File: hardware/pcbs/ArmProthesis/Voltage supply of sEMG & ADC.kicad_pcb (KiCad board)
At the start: 4 copper layers, 51.1 x 56.5 mm, 69 parts, among them Q1 BC817, Q2 BC817, Q3 BC817, U1 LT3045xMSE, U2 TPS7A4701RGWR, U3 LT8471EFE_TRPBF, U4 LT3094xMSE

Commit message: .
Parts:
- moved L3 0.99 mm to (117.3, 74.3)
- moved C5 0.98 mm to (118.0, 78.0)
- moved R17 0.30 mm to (112.9, 72.9)
- moved R1 0.29 mm to (103.5, 82.0)
- moved R15 0.12 mm to (121.7, 55.4)
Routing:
- net GND: track 85.2 -> 83.2 mm, vias 60 -> 57
- net Net-(U3-PG1): track 14.0 -> 13.4 mm

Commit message: BMS v0.5 still not resized
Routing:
- added copper zone on F.Cu, net Net-(U3-C3)
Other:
- board text added: "bigger gnd"
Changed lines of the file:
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@@
+		)
+	)
+	(gr_text "bigger gnd"
+		(at 120.26 81.055 0)
+		(layer "Cmts.User")
+		(effects
+			(font
+				(size 1.5 1.5)
+				(thickness 0.3)
+				(bold yes)
+			)
+			(justify left bottom)
 		)
 	)
@@
 	(segment
 		(start 128 79.75)
-		(end 129.65 79.75)
+		(end 130.55 79.75)
 		(width 0.3)
 		(layer "F.Cu")
@@
 	)
 	(segment
-		(start 129.9 80)
+		(start 130.55 79.75)
+		(end 130.8 80)
+		(width 0.3)
+		(layer "F.Cu")
+		(net 6)
+	)
+	(segment
+		(start 130.8 80)
 		(end 131.3325 80)
-		(width 0.3)
-		(layer "F.Cu")
-		(net 6)
-	)
-	(segment
-		(start 129.65 79.75)
-		(end 129.9 80)
 		(width 0.3)
 		(layer "F.Cu")
@@
 	)
 	(segment
+		(start 130.099596 80.44)
+		(end 129.44 80.44)
+		(width 0.3)
+		(layer "F.Cu")
+		(net 7)
+	)
+	(segment
+		(start 120.990364 77.649)
+		(end 119.909 77.649)
+		(width 0.3)
+		(layer "F.Cu")
+		(net 7)
+	)
+	(segment
+		(start 129.44 80.44)
+		(end 129.4 80.4)
+		(width 0.3)
+		(layer "F.Cu")
+		(net 7)
+	)
+	(segment
+		(start 121.141364 77.8)
+		(end 120.990364 77.649)
+		(width 0.3)
+		(layer "F.Cu")
+		(net 7)
+	)
+	(segment
+		(start 129.8 77.2)
+		(end 129.2 77.8)
+		(width 0.3)
+		(layer "F.Cu")
+		(net 7)
+	)
+	(segment
+		(start 119.624975 78.025025)
+		(end 118.899975 78.025025)
+		(width 0.3)
+		(layer "F.Cu")
+		(net 7)
+	)
+	(segment
+		(start 119.909 77.649)
+		(end 119.955 77.695)
+		(width 0.3)
+		(layer "F.Cu")
+		(net 7)
+	)
+	(segment
 		(start 129.4 80.4)
 		(end 128 80.4)
-		(width 0.3)
-		(layer "F.Cu")
-		(net 7)
-	)
-	(segment
-		(start 120.990364 77.649)
-		(end 119.909 77.649)
-		(width 0.3)
-		(layer "F.Cu")
-		(net 7)
-	)
-	(segment
-		(start 121.141364 77.8)
-		(end 120.990364 77.649)
-		(width 0.3)
-		(layer "F.Cu")
-		(net 7)
-	)
-	(segment
-		(start 129.8 77.2)
-		(end 129.2 77.8)
-		(width 0.3)
-		(layer "F.Cu")
-		(net 7)
-	)
-	(segment
-		(start 119.624975 78.025025)
-		(end 118.899975 78.025025)
-		(width 0.3)
-		(layer "F.Cu")
-		(net 7)
-	)
-	(segment
-		(start 119.909 77.649)
-		(end 119.955 77.695)
-		(width 0.3)
-		(layer "F.Cu")
-		(net 7)
-	)
-	(segment
-		(start 129.7 80.7)
-		(end 129.4 80.4)
 		(width 0.3)
 		(layer "F.Cu")
@@
 	)
 	(via
-		(at 129.7 80.7)
+		(at 130.099596 80.44)
 		(size 0.6)
 		(drill 0.3)
@@
 	)
 	(segment
+		(start 130.099596 80.44)
+		(end 130.099596 79.700404)
+		(width 0.3)
+		(layer "B.Cu")
+		(net 7)
+	)
+	(segment
+		(start 131.025 78.775)
+		(end 131.025 77.825)
+		(width 0.3)
+		(layer "B.Cu")
+		(net 7)
+	)
+	(segment
 		(start 129.975 77.2)
 		(end 129.375 77.8)
@@
 	)
 	(segment
-		(start 129.7 80.1)
+		(start 130.099596 79.700404)
 		(end 131.025 78.775)
+		(width 0.3)
+		(layer "B.Cu")
+		(net 7)
+	)
+	(segment
+		(start 131.025 77.825)
+		(end 130.4 77.2)
 		(width 0.3)
 		(layer "B.Cu")
@@
 	)
 	(segment
-		(start 129.7 80.7)
-		(end 129.7 80.1)
-		(width 0.3)
-		(layer "B.Cu")
-		(net 7)
-	)
-	(segment
 		(start 130.4 77.2)
 		(end 129.975 77.2)
-		(width 0.3)
-		(layer "B.Cu")
-		(net 7)
-	)
-	(segment
-		(start 131.025 78.775)
-		(end 131.025 77.825)
-		(width 0.3)
-		(layer "B.Cu")
-		(net 7)
-	)
-	(segment
-		(start 131.025 77.825)
-		(end 130.4 77.2)
 		(width 0.3)
 		(layer "B.Cu")
@@
 	)
 	(zone
+		(net 22)
+		(net_name "Net-(U3-C3)")
+		(layer "F.Cu")
+		(hatch edge 0.5)
+		(priority 1)
+		(connect_pads yes
+			(clearance 0)
+		)
+		(min_thickness 0.25)
+		(filled_areas_thickness no)
+		(fill yes
+			(thermal_gap 0.5)
+			(thermal_bridge_width 0.5)
+		)
+		(polygon
+			(pts
+				(xy 127.225 80.8) (xy 127.225 81.275) (xy 129.3 81.275) (xy 129.3 84.975) (xy 138.6 85) (xy 138.6 80.8)
+			)
+		)
+	)
+	(zone

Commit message: .
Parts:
- moved R4 4.12 mm to (111.3, 79.5), turned to -90 degrees
- moved C6 2.26 mm to (122.3, 70.8), turned to 0 degrees
- moved Cby5 2.04 mm to (128.5, 61.6)
- moved C7 1.18 mm to (127.6, 70.8)
- moved R20 0.95 mm to (122.5, 62.5), turned to 0 degrees
- moved C9 0.92 mm to (127.7, 72.8)
- moved C8 0.79 mm to (122.3, 72.8), turned to 0 degrees
- moved R25 0.45 mm to (112.9, 77.7)
- moved C2in1 0.21 mm to (113.4, 68.2)
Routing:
- net Net-(U3-FB2): track 12.1 -> 0.00 mm
- net /+5V: track 42.4 -> 32.3 mm
- net /+11.1V: track 10.7 -> 6.94 mm
- net GND: track 83.2 -> 79.8 mm, vias 57 -> 63
- net +6V: track 72.7 -> 70.6 mm, vias 4 -> 3
- net Net-(U1-PGFB): track 12.4 -> 14.4 mm
- net Net-(U3-PG1): track 13.4 -> 14.3 mm
- net Net-(U4-PGFB): track 18.6 -> 19.3 mm
- net Net-(U3-PG2): track 17.2 -> 16.5 mm
- added copper zone on F.Cu, net -6V
- added copper zone on F.Cu, net /+5V
- added copper zone on F.Cu, net GND
- added copper zone on F.Cu, net Net-(U3-E1)
- added copper zone on F.Cu, net Net-(U3-FB2)
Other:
- board text added: "SL-sEMG&ADC-PSU v0.5"
- board text removed: "SL-sEMG&ADC-PSU v0.4"
- board text removed: "bigger gnd"

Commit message: updates
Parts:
- added D8: DFLS240L, Diode_SMD:D_PowerDI-123, F.Cu at (88.6, 68.8)
- added D9: DFLS240, Diode_SMD:D_PowerDI-123, F.Cu at (131.4, 63.6)
- C1, Cby1, Cby3, Cby5, Cby7: value 10u -> 10uF
- C2, C3: value 100n -> 100nF
- Cby4: value 47u -> 47uF
- moved D7 1.71 mm to (136.6, 63.3)
- moved R22 1.71 mm to (133.0, 63.3)
- moved R15 1.30 mm to (123.0, 55.4)
- moved Cby6 1.03 mm to (124.8, 55.4)
- moved Cby5 0.41 mm to (128.1, 61.6)
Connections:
- L2 pad 2: -6V -> Net-(D9-K)
- R16 pad 1: -6V -> Net-(D9-K)
- U1 pad 12: /+5V -> Net-(U1-PG)
- U3 pad 19: -6V -> Net-(D9-K)
- U4 pad 12: /-5.5V -> Net-(U4-PG)
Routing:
- net GND: track 79.8 -> 76.4 mm, vias 63 -> 68
- net Net-(U4-SET): track 5.79 -> 4.73 mm

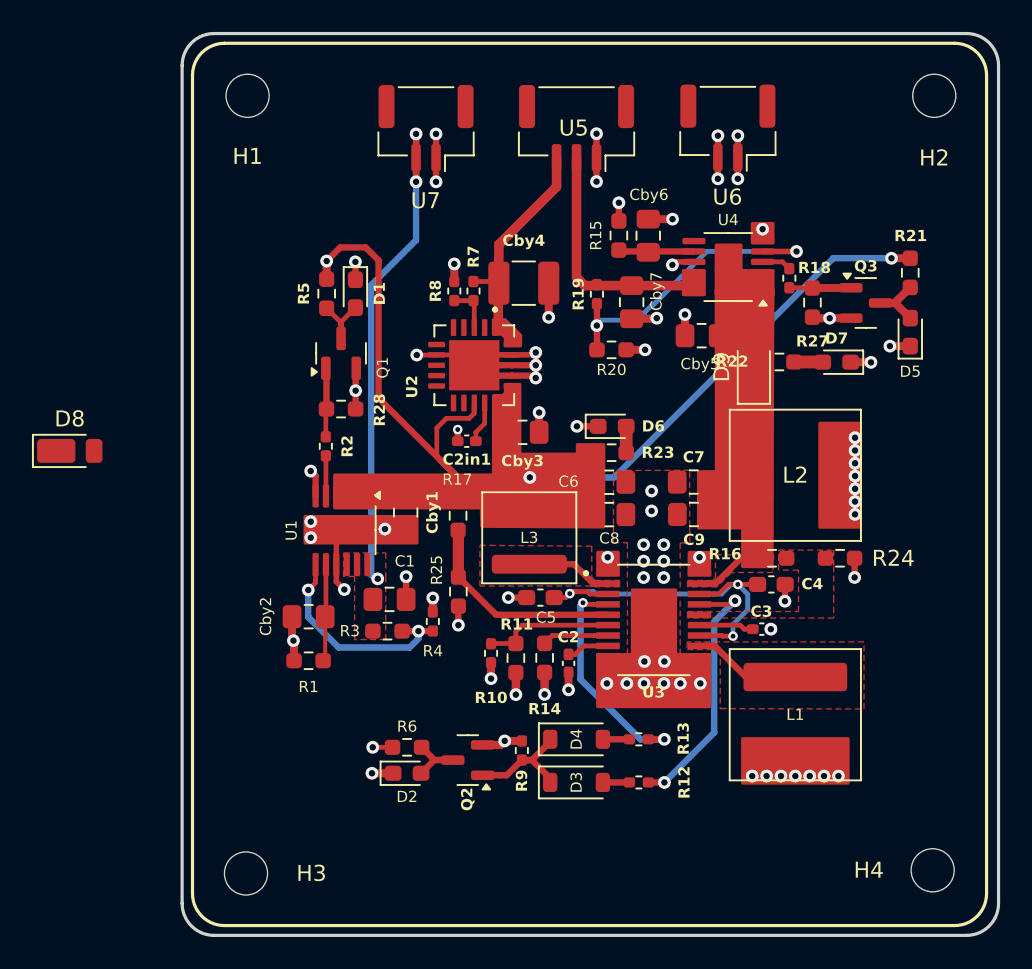
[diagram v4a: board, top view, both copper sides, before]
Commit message: Fix Vsupply
added important Schottky diodes on the BUCK
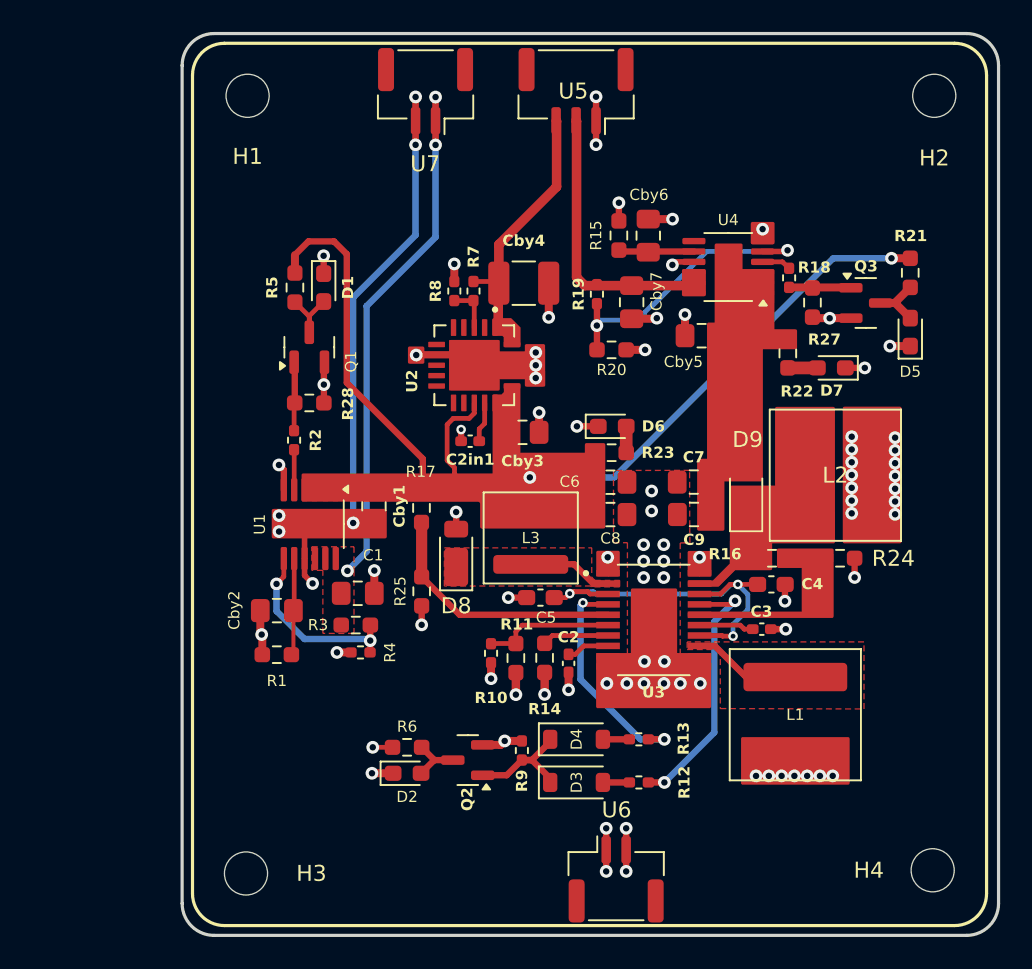
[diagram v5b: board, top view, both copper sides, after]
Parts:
- moved U6 47.6 mm to (122.8, 95.7), turned to 0 degrees
- moved D8 25.0 mm to (112.8, 75.3), turned to 90 degrees
- moved D9 7.99 mm to (130.9, 71.6)
- moved R4 4.93 mm to (106.8, 81.5), turned to 0 degrees
- moved L2 2.51 mm to (136.5, 70.4)
- moved R17 2.34 mm to (110.6, 72.4)
- moved U5 2.32 mm to (120.3, 46.3)
- moved U7 2.32 mm to (110.8, 46.3)
- moved R25 2.30 mm to (110.6, 77.6)
- moved C1 2.02 mm to (106.6, 77.8)
- moved R3 2.02 mm to (106.5, 79.7)
- moved R5 2.02 mm to (102.7, 58.6)
- moved R1 2.02 mm to (101.5, 81.6)
- moved U1 2.02 mm to (103.6, 73.4)
- moved Q1 2.02 mm to (103.6, 62.3)
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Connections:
- U1 pad 12: Net-(U1-PG) -> /+5V
- U4 pad 12: Net-(U4-PG) -> /-5.5V
- U7 pad 1: GND -> /+5V
- U7 pad 2: /+5V -> GND
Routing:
- net GND: track 76.4 -> 85.8 mm, vias 68 -> 76
- net +6V: track 70.6 -> 61.9 mm, vias 3 -> 2
- net -6V: track 4.29 -> 0.00 mm
- net Net-(U1-PGFB): track 14.4 -> 11.6 mm
- net Net-(U3-FB1): track 13.3 -> 16.0 mm
- net /+5V: track 32.3 -> 35.0 mm
- net /-5.5V: track 14.8 -> 17.1 mm
- net Net-(U4-PGFB): track 19.3 -> 18.3 mm
- removed copper zone on F.Cu, net -6V
- removed copper zone on F.Cu, net Net-(U3-FB2)
